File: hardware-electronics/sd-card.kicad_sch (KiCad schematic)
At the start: 39 parts, among them J2 Micro_SD_Card_Det_Hirose_DM3AT, U6 24AA04T-I_OT, U9 USB2244-AEZG-06, Y3 ECS-240-10-47-CKM-TR

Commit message: SCH fill info box
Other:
- title: (none) -> M2SmartHome
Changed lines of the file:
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@@
 	(generator_version "8.0")
 	(paper "A4")
+	(title_block
+		(title "M2SmartHome")
+		(date "2024-10-11")
+		(rev "Rev 1.0.0")
+	)
 	(junction
 		(at 107.95 76.2)

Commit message: SCH update all symbols
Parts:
- C20, C25: footprint C_4pF_0402:C_0402_1005Metric -> M2SmartHomeFootprints:C_0402
- C24, C27, C29, C31, C33, C35, C39: footprint C_100n_0402:C_0402_1005Metric -> M2SmartHomeFootprints:C_0402
- C26, C28, C30, C32, C34, C36, C37: footprint C_1uF_0402:C_0402_1005Metric -> M2SmartHomeFootprints:C_0201
- C38: footprint C_4u7_0402:C_0402_1005Metric -> M2SmartHomeFootprints:C_0402
- FB5: footprint FB_120R_0603:FB_0603_1608Metric -> M2SmartHomeFootprints:FB_0603
- R21, R22, R24, R25, R32: footprint R_49k9_0402:R_0402_1005Metric -> M2SmartHomeFootprints:R_0402
- R23, R26: footprint R_4k7_0402:R_0402_1005Metric -> M2SmartHomeFootprints:R_0402
- R27, R28: footprint R_500R_0402:R_0402_1005Metric -> M2SmartHomeFootprints:R_0402
- R33, R37, R39: footprint R_10k_0402:R_0402_1005Metric -> M2SmartHomeFootprints:R_0402
- R34: footprint R_0_0402:R_0402_1005Metric -> M2SmartHomeFootprints:R_0402
- R35: footprint R_1M_0402:R_0402_1005Metric -> M2SmartHomeFootprints:R_0402
- R36: footprint R_12k_0402:R_0402_1005Metric -> M2SmartHomeFootprints:R_0402
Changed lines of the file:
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@@
 			)
 		)
-		(property "Footprint" "R_49k9_0402:R_0402_1005Metric"
+		(property "Footprint" "M2SmartHomeFootprints:R_0402"
 			(at 128.27 48.26 0)
 			(effects
@@
 			)
 		)
-		(property "Footprint" "R_49k9_0402:R_0402_1005Metric"
+		(property "Footprint" "M2SmartHomeFootprints:R_0402"
 			(at 123.19 48.26 0)
 			(effects
@@
 			)
 		)
-		(property "Footprint" "C_1uF_0402:C_0402_1005Metric"
+		(property "Footprint" "M2SmartHomeFootprints:C_0201"
 			(at 205.74 86.36 0)
 			(effects
@@
 			)
 		)
-		(property "Footprint" "R_1M_0402:R_0402_1005Metric"
+		(property "Footprint" "M2SmartHomeFootprints:R_0402"
 			(at 60.96 163.83 0)
 			(effects
@@
 			)
 		)
-		(property "Footprint" "R_500R_0402:R_0402_1005Metric"
+		(property "Footprint" "M2SmartHomeFootprints:R_0402"
 			(at 175.26 59.69 0)
 			(effects
@@
 			)
 		)
-		(property "Footprint" "R_49k9_0402:R_0402_1005Metric"
+		(property "Footprint" "M2SmartHomeFootprints:R_0402"
 			(at 118.11 48.26 0)
 			(effects
@@
 			)
 		)
-		(property "Footprint" "C_100n_0402:C_0402_1005Metric"
+		(property "Footprint" "M2SmartHomeFootprints:C_0402"
 			(at 240.03 78.74 0)
 			(effects
@@
 			)
 		)
-		(property "Footprint" "C_4pF_0402:C_0402_1005Metric"
+		(property "Footprint" "M2SmartHomeFootprints:C_0402"
 			(at 46.99 137.16 0)
 			(effects
@@
 			)
 		)
-		(property "Footprint" "C_1uF_0402:C_0402_1005Metric"
+		(property "Footprint" "M2SmartHomeFootprints:C_0201"
 			(at 91.44 60.96 0)
 			(effects
@@
 			)
 		)
-		(property "Footprint" "C_4u7_0402:C_0402_1005Metric"
+		(property "Footprint" "M2SmartHomeFootprints:C_0402"
 			(at 127 87.63 0)
 			(effects
@@
 			)
 		)
-		(property "Footprint" "R_10k_0402:R_0402_1005Metric"
+		(property "Footprint" "M2SmartHomeFootprints:R_0402"
 			(at 93.98 52.07 0)
 			(effects
@@
 			)
 		)
-		(property "Footprint" "C_100n_0402:C_0402_1005Metric"
+		(property "Footprint" "M2SmartHomeFootprints:C_0402"
 			(at 222.25 78.74 0)
 			(effects
@@
 			)
 		)
-		(property "Footprint" "R_4k7_0402:R_0402_1005Metric"
+		(property "Footprint" "M2SmartHomeFootprints:R_0402"
 			(at 96.52 173.99 0)
 			(effects
@@
 			)
 		)
-		(property "Datasheet" ""
+		(property "Datasheet" "https://ww1.microchip.com/downloads/aemDocuments/documents/MPD/ProductDocuments/DataSheets/24AA04-24LC04B-24FC04-4K-I2C-Serial-EEPROM-20001708P.pdf"
 			(at 142.24 166.37 0)
 			(effects
@@
 			)
 		)
-		(property "Footprint" "R_500R_0402:R_0402_1005Metric"
+		(property "Footprint" "M2SmartHomeFootprints:R_0402"
 			(at 111.76 93.98 0)
 			(effects
@@
 			)
 		)
-		(property "Footprint" "R_49k9_0402:R_0402_1005Metric"
+		(property "Footprint" "M2SmartHomeFootprints:R_0402"
 			(at 113.03 48.26 0)
 			(effects
@@
 			)
 		)
-		(property "Footprint" "R_49k9_0402:R_0402_1005Metric"
+		(property "Footprint" "M2SmartHomeFootprints:R_0402"
 			(at 134.62 48.26 0)
 			(effects
@@
 			)
 		)
-		(property "Footprint" "FB_120R_0603:FB_0603_1608Metric"
+		(property "Footprint" "M2SmartHomeFootprints:FB_0603"
 			(at 259.08 101.6 0)
 			(effects
@@
 			)
 		)
-		(property "Footprint" "C_1uF_0402:C_0402_1005Metric"
+		(property "Footprint" "M2SmartHomeFootprints:C_0201"
 			(at 271.78 74.93 0)
 			(effects
@@
 			)
 		)
-		(property "Footprint" "C_1uF_0402:C_0402_1005Metric"
+		(property "Footprint" "M2SmartHomeFootprints:C_0201"
 			(at 288.29 68.58 0)
 			(effects
@@
 			)
 		)
-		(property "Footprint" "C_4pF_0402:C_0402_1005Metric"
+		(property "Footprint" "M2SmartHomeFootprints:C_0402"
 			(at 63.5 137.16 0)
 			(effects
@@
 			)
 		)
-		(property "Footprint" "R_0_0402:R_0402_1005Metric"
+		(property "Footprint" "M2SmartHomeFootprints:R_0402"
 			(at 143.51 86.36 0)
 			(effects
@@
 			)
 		)
-		(property "Footprint" "R_10k_0402:R_0402_1005Metric"
+		(property "Footprint" "M2SmartHomeFootprints:R_0402"
 			(at 138.43 48.26 0)
 			(effects
@@
 			)
 		)
-		(property "Footprint" "R_10k_0402:R_0402_1005Metric"
+		(property "Footprint" "M2SmartHomeFootprints:R_0402"
 			(at 99.06 142.24 0)
 			(effects
@@
 			)
 		)
-		(property "Footprint" "C_100n_0402:C_0402_1005Metric"
+		(property "Footprint" "M2SmartHomeFootprints:C_0402"
 			(at 118.11 87.63 0)
 			(effects
@@
 			)
 		)
-		(property "Footprint" "R_12k_0402:R_0402_1005Metric"
+		(property "Footprint" "M2SmartHomeFootprints:R_0402"
 			(at 191.77 90.17 0)
 			(effects
@@
 			)
 		)
-		(property "Footprint" "C_100n_0402:C_0402_1005Metric"
+		(property "Footprint" "M2SmartHomeFootprints:C_0402"
 			(at 279.4 68.58 0)
 			(effects
@@
 			)
 		)
-		(property "Footprint" "C_100n_0402:C_0402_1005Metric"
+		(property "Footprint" "M2SmartHomeFootprints:C_0402"
 			(at 262.89 74.93 0)
 			(effects
@@
 			)
 		)
-		(property "Footprint" "C_1uF_0402:C_0402_1005Metric"
+		(property "Footprint" "M2SmartHomeFootprints:C_0201"
 			(at 248.92 78.74 0)
 			(effects
@@
 			)
 		)
-		(property "Footprint" "C_100n_0402:C_0402_1005Metric"
+		(property "Footprint" "M2SmartHomeFootprints:C_0402"
 			(at 175.26 142.24 0)
 			(effects
@@
 			)
 		)
-		(property "Footprint" "C_100n_0402:C_0402_1005Metric"
+		(property "Footprint" "M2SmartHomeFootprints:C_0402"
 			(at 196.85 86.36 0)
 			(effects
@@
 			)
 		)
-		(property "Footprint" "C_1uF_0402:C_0402_1005Metric"
+		(property "Footprint" "M2SmartHomeFootprints:C_0201"
 			(at 96.52 154.94 0)
 			(effects
@@
 			)
 		)
-		(property "Footprint" "C_1uF_0402:C_0402_1005Metric"
+		(property "Footprint" "M2SmartHomeFootprints:C_0201"
 			(at 231.14 78.74 0)
 			(effects
@@
 			)
 		)
-		(property "Footprint" "R_4k7_0402:R_0402_1005Metric"
+		(property "Footprint" "M2SmartHomeFootprints:R_0402"
 			(at 137.16 138.43 0)
 			(effects

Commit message: [#13] BRD fix 66k5 r and uSD slot
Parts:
- J2: footprint (none) -> M2SmartHomeFootprints:HRS_DM3AT-SF-PEJM5
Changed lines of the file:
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@@
 			)
 		)
-		(property "Footprint" ""
+		(property "Footprint" "M2SmartHomeFootprints:HRS_DM3AT-SF-PEJM5"
 			(at -10.16 105.41 0)
 			(effects

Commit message: [#13] WIP Placement wifi
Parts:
- C26, C28, C30, C32, C34, C36, C37: footprint M2SmartHomeFootprints:C_0201 -> M2SmartHomeFootprints:C_0402
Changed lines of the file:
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@@
 			)
 		)
-		(property "Footprint" "M2SmartHomeFootprints:C_0201"
+		(property "Footprint" "M2SmartHomeFootprints:C_0402"
 			(at 205.74 86.36 0)
 			(effects
@@
 			)
 		)
-		(property "Footprint" "M2SmartHomeFootprints:C_0201"
+		(property "Footprint" "M2SmartHomeFootprints:C_0402"
 			(at 91.44 60.96 0)
 			(effects
@@
 			)
 		)
-		(property "Footprint" "M2SmartHomeFootprints:C_0201"
+		(property "Footprint" "M2SmartHomeFootprints:C_0402"
 			(at 271.78 74.93 0)
 			(effects
@@
 			)
 		)
-		(property "Footprint" "M2SmartHomeFootprints:C_0201"
+		(property "Footprint" "M2SmartHomeFootprints:C_0402"
 			(at 288.29 68.58 0)
 			(effects
@@
 			)
 		)
-		(property "Footprint" "M2SmartHomeFootprints:C_0201"
+		(property "Footprint" "M2SmartHomeFootprints:C_0402"
 			(at 248.92 78.74 0)
 			(effects
@@
 			)
 		)
-		(property "Footprint" "M2SmartHomeFootprints:C_0201"
+		(property "Footprint" "M2SmartHomeFootprints:C_0402"
 			(at 96.52 154.94 0)
 			(effects
@@
 			)
 		)
-		(property "Footprint" "M2SmartHomeFootprints:C_0201"
+		(property "Footprint" "M2SmartHomeFootprints:C_0402"
 			(at 231.14 78.74 0)
 			(effects

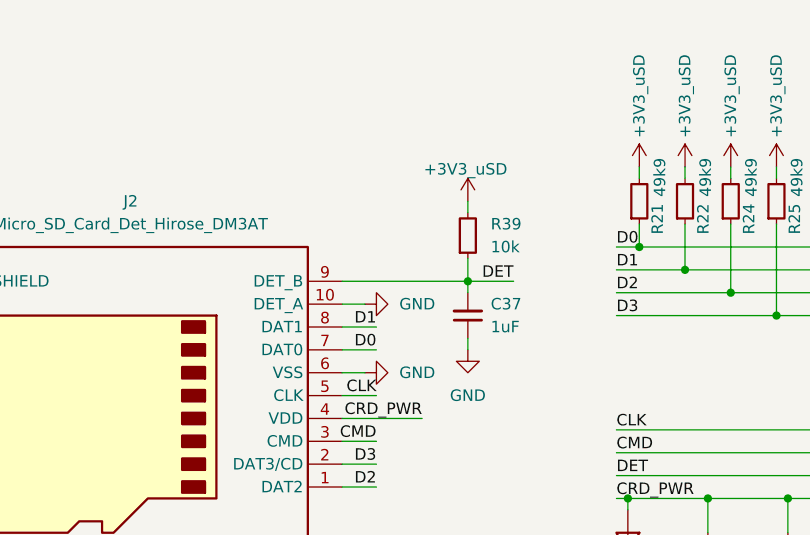
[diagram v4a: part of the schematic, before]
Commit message: [#16] Add 100ohm resistor for SD card det
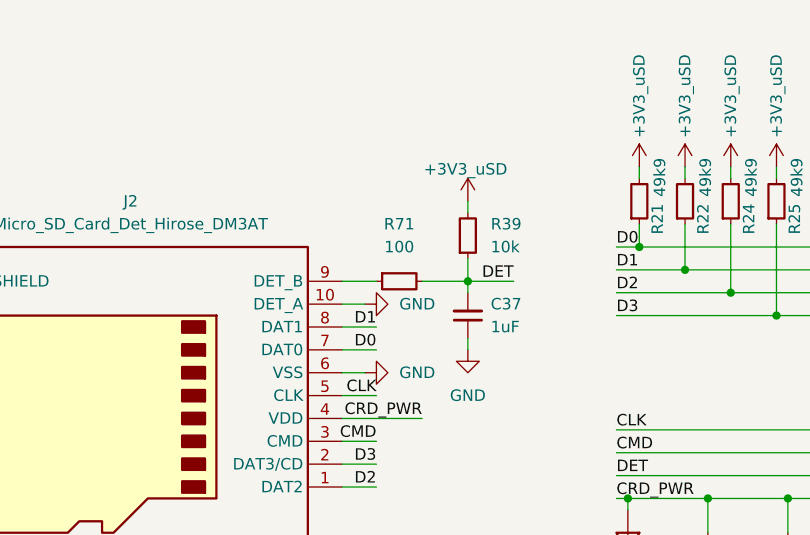
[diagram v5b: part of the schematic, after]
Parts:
- added R71: R_100_0402, M2SmartHomeFootprints:R_0402, symbol M2SmartHomeSymbols:R_100_0402
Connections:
- net DET: now also R71.2; no longer J2.9 (DET_B)
- new net: J2.9 (DET_B), R71.1
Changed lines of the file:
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@@
 	(wire
 		(pts
-			(xy 64.77 74.93) (xy 78.74 74.93)
-		)
-		(stroke
-			(width 0)
-			(type default)
-		)
-	)
-	(wire
-		(pts
 			(xy 96.52 114.3) (xy 96.52 115.57)
 		)
@@
 	(wire
 		(pts
+			(xy 64.77 74.93) (xy 68.58 74.93)
+		)
+		(stroke
+			(width 0)
+			(type default)
+		)
+	)
+	(wire
+		(pts
+			(xy 73.66 74.93) (xy 78.74 74.93)
+		)
+		(stroke
+			(width 0)
+			(type default)
+		)
+	)
+	(wire
+		(pts
 			(xy 113.03 62.23) (xy 113.03 63.5)
 		)
@@
 					(unit 1)
 				)
+			)
+		)
+	)
+	(symbol
+		(lib_id "M2SmartHomeSymbols:R_100_0402")
+		(at 68.58 74.93 0)
+		(unit 1)
+		(exclude_from_sim no)
+		(in_bom yes)
+		(on_board yes)
+		(dnp no)
+		(fields_autoplaced yes)
+		(property "Reference" "R71"
+			(at 71.12 68.58 0)
+			(effects
+				(font
+					(size 1.27 1.27)
+					(thickness 0.15)
+				)
+			)
+		)
+		(property "Value" "R_100_0402"
+			(at 88.9 87.63 0)
+			(effects
+				(font
+					(size 1.27 1.27)
+					(thickness 0.15)
+				)
+				(justify left bottom)
+				(hide yes)
+			)
+		)
+		(property "Footprint" "M2SmartHomeFootprints:R_0402"
+			(at 88.9 90.17 0)
+			(effects
+				(font
+					(size 1.27 1.27)
+					(thickness 0.15)
+				)
+				(justify left bottom)
+				(hide yes)
+			)
+		)
+		(property "Datasheet" "https://www.vishay.com/docs/20035/crcw0402.pdf"
+			(at 88.9 92.71 0)
+			(effects
+				(font
+					(size 1.27 1.27)
+					(thickness 0.15)
+				)
+				(justify left bottom)
+				(hide yes)
+			)
+		)
+		(property "Description" "SMD Thick Film Resistor, 100 Ω, ±1%, 1/16 W, 0402 [1005 Metric], CRCW Series"
+			(at 68.58 74.93 0)
+			(effects
+				(font
+					(size 1.27 1.27)
+				)
+				(hide yes)
+			)
+		)
+		(property "MPN" "CRCW0402100RFKED"
+			(at 88.9 95.25 0)
+			(effects
+				(font
+					(size 1.27 1.27)
+					(thickness 0.15)
+				)
+				(justify left bottom)
+				(hide yes)
+			)
+		)
+		(property "Manufacturer" "Vishay"
+			(at 88.9 97.79 0)
+			(effects
+				(font
+					(size 1.27 1.27)
+					(thickness 0.15)
+				)
+				(justify left bottom)
+				(hide yes)
+			)
+		)
+		(property "License" "Apache-2.0"
+			(at 88.9 100.33 0)
+			(effects
+				(font
+					(size 1.27 1.27)
+					(thickness 0.15)
+				)
+				(justify left bottom)
+				(hide yes)
+			)
+		)
+		(property "Val" "100"
+			(at 71.12 71.12 0)
+			(effects
+				(font
+					(size 1.27 1.27)
+					(thickness 0.15)
+				)
+			)
+		)
+		(property "Tolerance" "1%"
+			(at 88.9 85.09 0)
+			(effects
+				(font
+					(size 1.27 1.27)
+				)
+				(justify left bottom)
+				(hide yes)
+			)
+		)
+		(property "Power" "1/16 W"
+			(at 88.9 88.63 0)
+			(effects
+				(font
+					(size 1.27 1.27)
+				)
+				(justify left bottom)
+				(hide yes)
+			)
+		)
+		(pin "1"
+		)
+		(pin "2"
+		)
+		(instances
+			(project "M2SmartHome"
+				(path "/da663dec-9e91-4003-a791-431d460ad63c/2a53ffe2-5715-44b3-b464-b3185e5be86d"
+					(reference "R71")
+					(unit 1)
+				)

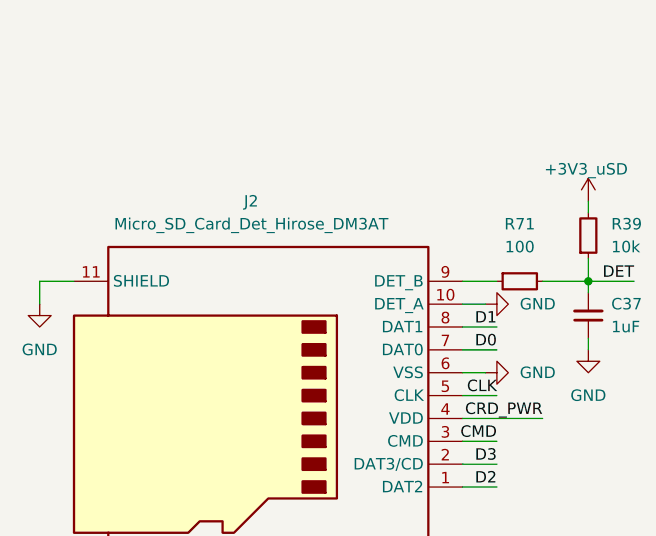
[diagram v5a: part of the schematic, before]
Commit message: [#16] Fix uSD reader symbol
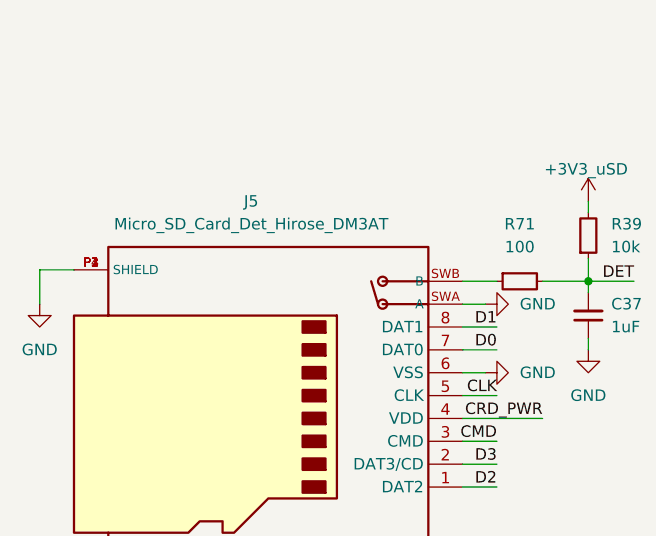
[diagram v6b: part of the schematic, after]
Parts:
- removed J2: Micro_SD_Card_Det_Hirose_DM3AT, M2SmartHomeFootprints:HRS_DM3AT-SF-PEJM5, symbol Connector:Micro_SD_Card_Det_Hirose_DM3AT
- added J5: Micro_SD_Card_Det_Hirose_DM3AT, M2SmartHomeFootprints:HRS_DM3AT-SF-PEJM5, symbol M2SmartHomeSymbols:Micro_SD_Card_Det_Hirose_DM3AT
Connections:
- net CLK: now also J5.5 (CLK)
- net CMD: now also J5.3 (CMD)
- net CRD_PWR: now also J5.4 (VDD)
- net D0: now also J5.7 (DAT0)
- net D1: now also J5.8 (DAT1)
- net D2: now also J5.1 (DAT2)
- net D3: now also J5.2 (DAT3/CD)
- net GND: now also J5.6 (VSS), J5.P1 (SHIELD), J5.P2 (SHIELD), J5.P3 (SHIELD), J5.P4 (SHIELD), J5.SWA (A)
- net at R71.1: now also J5.SWB (B)
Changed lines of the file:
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@@
 	(wire
 		(pts
-			(xy 21.59 74.93) (xy 17.78 74.93)
+			(xy 21.59 73.66) (xy 17.78 73.66)
 		)
 		(stroke
@@
 	(wire
 		(pts
-			(xy 17.78 74.93) (xy 17.78 77.47)
+			(xy 17.78 73.66) (xy 17.78 77.47)
 		)
 		(stroke
@@
 	)
 	(symbol
+		(lib_id "M2SmartHomeSymbols:Micro_SD_Card_Det_Hirose_DM3AT")
+		(at 41.91 87.63 180)
+		(unit 1)
+		(exclude_from_sim no)
+		(in_bom yes)
+		(on_board yes)
+		(dnp no)
+		(fields_autoplaced yes)
+		(property "Reference" "J5"
+			(at 41.275 66.04 0)
+			(effects
+				(font
+					(size 1.27 1.27)
+				)
+			)
+		)
+		(property "Value" "Micro_SD_Card_Det_Hirose_DM3AT"
+			(at 41.275 68.58 0)
+			(effects
+				(font
+					(size 1.27 1.27)
+				)
+			)
+		)
+		(property "Footprint" "M2SmartHomeFootprints:HRS_DM3AT-SF-PEJM5"
+			(at -10.16 105.41 0)
+			(effects
+				(font
+					(size 1.27 1.27)
+				)
+				(hide yes)
+			)
+		)
+		(property "Datasheet" "https://www.hirose.com/product/en/download_file/key_name/DM3/category/Catalog/doc_file_id/49662/?file_category_id=4&item_id=195&is_series=1"
+			(at 41.91 90.17 0)
+			(effects
+				(font
+					(size 1.27 1.27)
+				)
+				(hide yes)
+			)
+		)
+		(property "Description" "Micro SD Card Socket with card detection pins"
+			(at 41.91 87.63 0)
+			(effects
+				(font
+					(size 1.27 1.27)
+				)
+				(hide yes)
+			)
+		)
+		(pin "2"
+		)
+		(pin "P1"
+		)
+		(pin "SWB"
+		)
+		(pin "P3"
+		)
+		(pin "4"
+		)
+		(pin "5"
+		)
+		(pin "1"
+		)
+		(pin "6"
+		)
+		(pin "7"
+		)
+		(pin "8"
+		)
+		(pin "P4"
+		)
+		(pin "P2"
+		)
+		(pin "3"
+		)
+		(pin "SWA"
+		)
+		(instances
+			(project "M2SmartHome"
+				(path "/da663dec-9e91-4003-a791-431d460ad63c/2a53ffe2-5715-44b3-b464-b3185e5be86d"
+					(reference "J5")
+					(unit 1)
+				)
+			)
+		)
+	)
+	(symbol
 		(lib_id "M2SmartHomeSymbols:USB2244-AEZG-06")
 		(at 157.48 72.39 0)
@@
 					(unit 1)
 				)
-			)
-		)
-	)
-	(symbol
-		(lib_id "Connector:Micro_SD_Card_Det_Hirose_DM3AT")
-		(at 41.91 87.63 180)
-		(unit 1)
-		(exclude_from_sim no)
-		(in_bom yes)
-		(on_board yes)
-		(dnp no)
-		(fields_autoplaced yes)
-		(property "Reference" "J2"
-			(at 41.275 66.04 0)
-			(effects
-				(font
-					(size 1.27 1.27)
-				)
-			)
-		)
-		(property "Value" "Micro_SD_Card_Det_Hirose_DM3AT"
-			(at 41.275 68.58 0)
-			(effects
-				(font
-					(size 1.27 1.27)
-				)
-			)
-		)
-		(property "Footprint" "M2SmartHomeFootprints:HRS_DM3AT-SF-PEJM5"
-			(at -10.16 105.41 0)
-			(effects
-				(font
-					(size 1.27 1.27)
-				)
-				(hide yes)
-			)
-		)
-		(property "Datasheet" "https://www.hirose.com/product/en/download_file/key_name/DM3/category/Catalog/doc_file_id/49662/?file_category_id=4&item_id=195&is_series=1"
-			(at 41.91 90.17 0)
-			(effects
-				(font
-					(size 1.27 1.27)
-				)
-				(hide yes)
-			)
-		)
-		(property "Description" "Micro SD Card Socket with card detection pins"
-			(at 41.91 87.63 0)
-			(effects
-				(font
-					(size 1.27 1.27)
-				)
-				(hide yes)
-			)
-		)
-		(pin "5"
-		)
-		(pin "10"
-		)
-		(pin "8"
-		)
-		(pin "11"
-		)
-		(pin "9"
-		)
-		(pin "7"
-		)
-		(pin "3"
-		)
-		(pin "6"
-		)
-		(pin "4"
-		)
-		(pin "1"
-		)
-		(pin "2"
-		)
-		(instances
-			(project "M2SmartHome"
-				(path "/da663dec-9e91-4003-a791-431d460ad63c/2a53ffe2-5715-44b3-b464-b3185e5be86d"
-					(reference "J2")
-					(unit 1)
-				)
